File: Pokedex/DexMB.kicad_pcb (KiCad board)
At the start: 2 copper layers, 155.9 x 78.9 mm, 85 parts

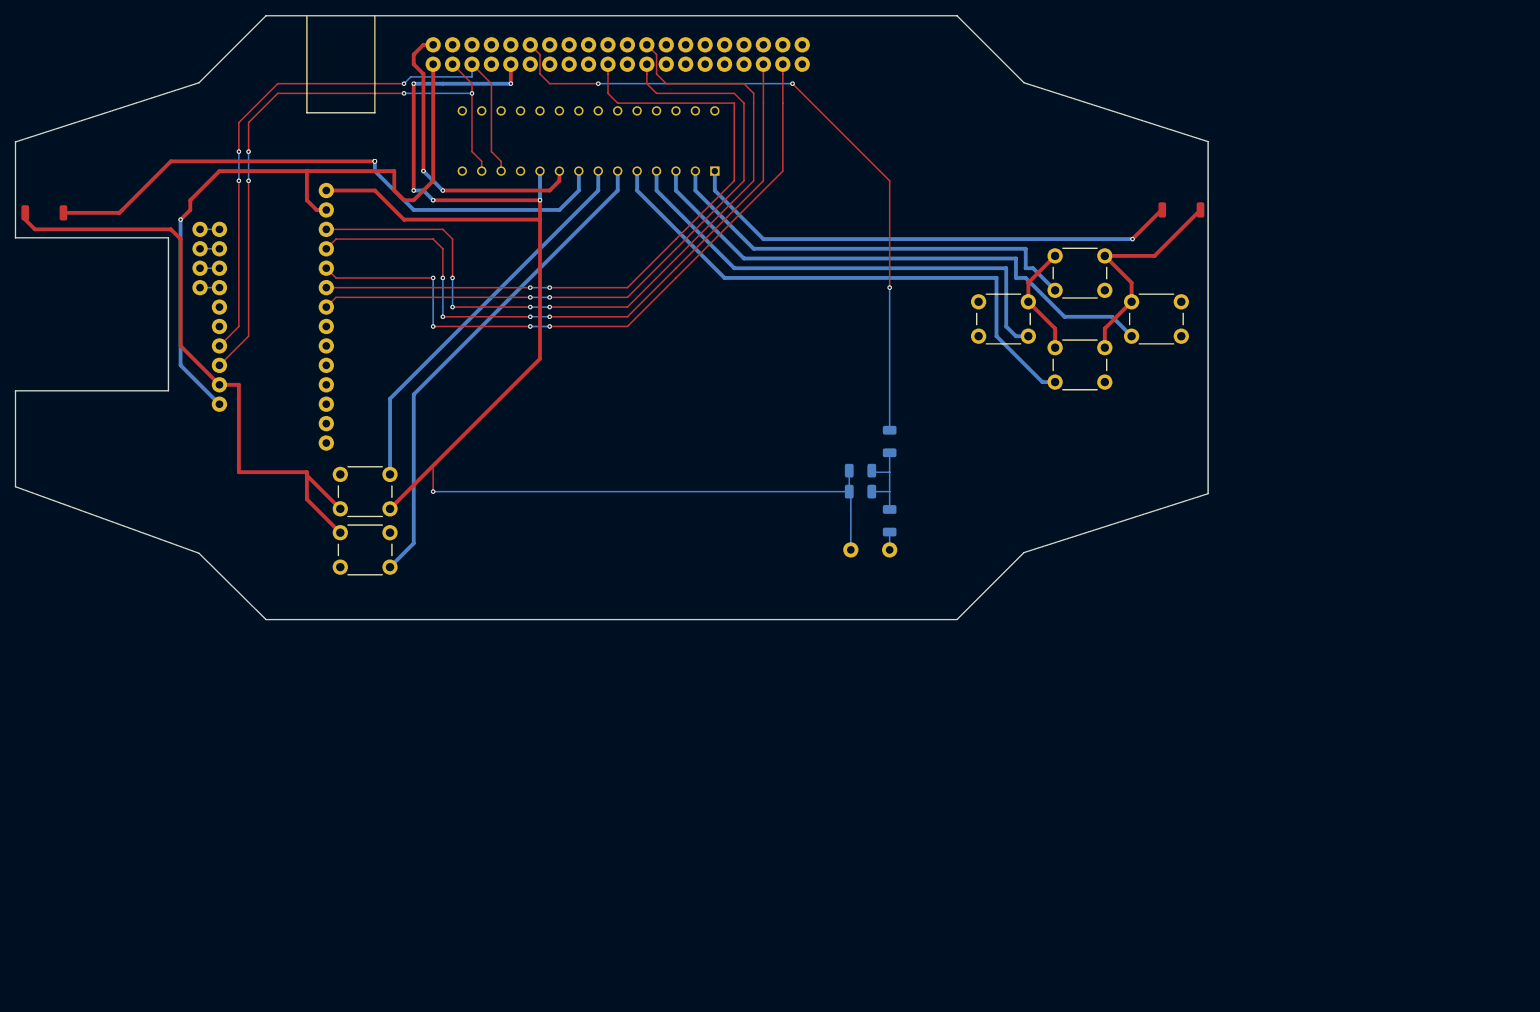
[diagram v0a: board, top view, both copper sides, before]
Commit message: Complete redesign progress and slimming of Motherboard
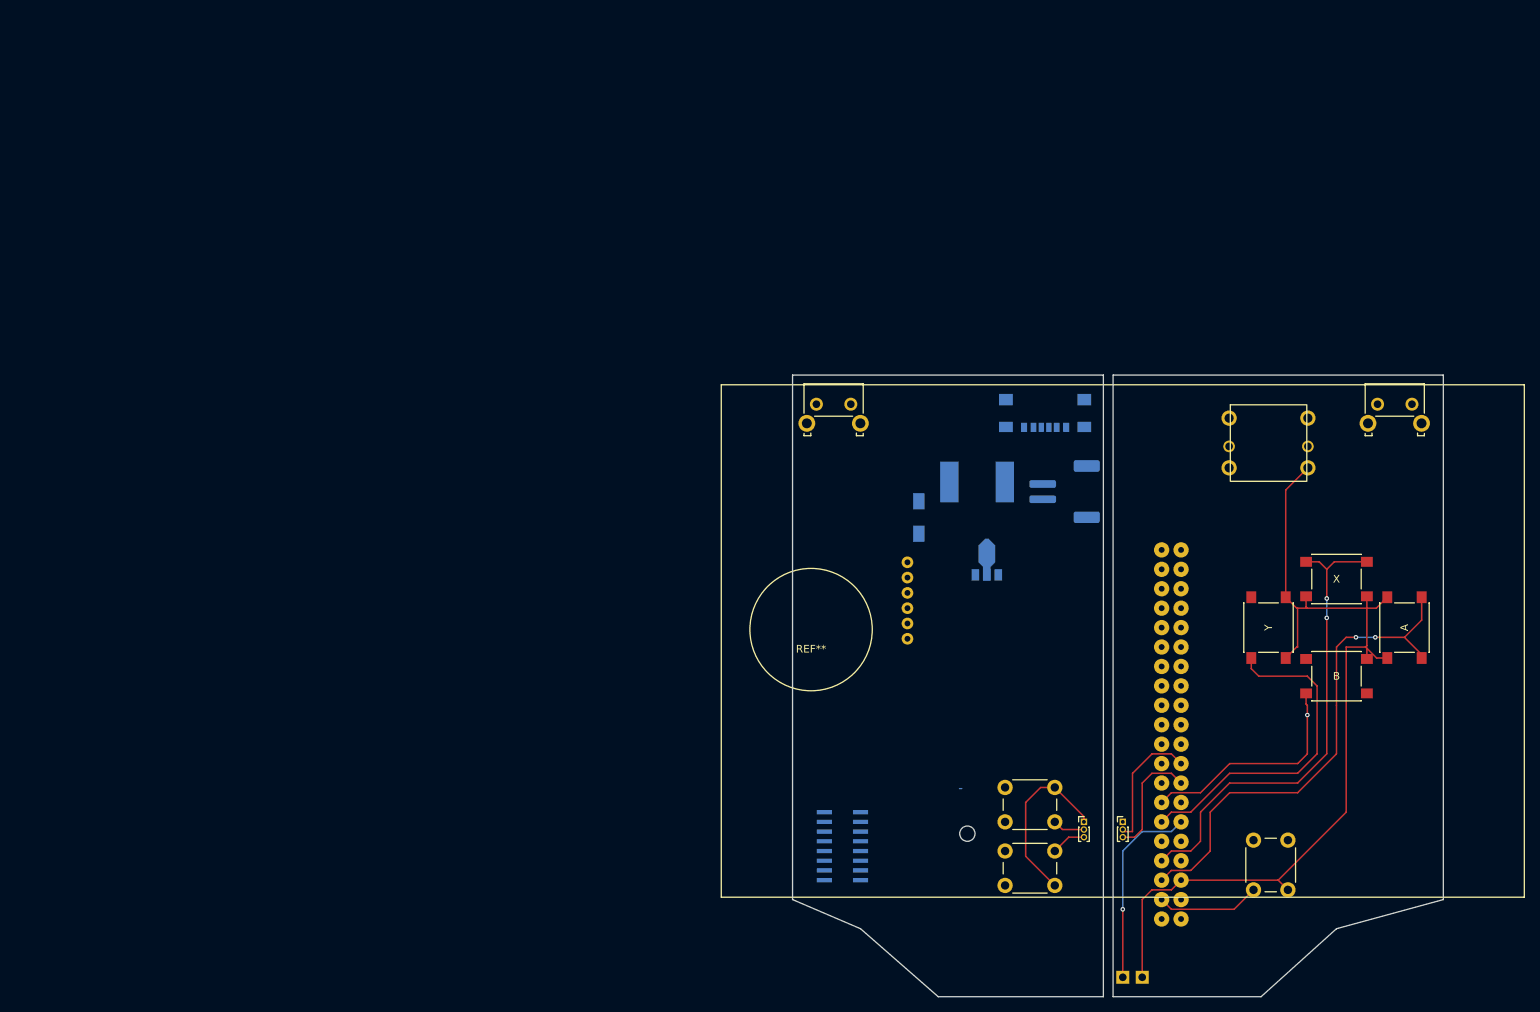
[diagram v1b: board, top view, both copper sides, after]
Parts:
- removed the ? at (39.4, 58.4)
- removed the ? at (36.8, 45.7)
- removed the ? at (92.7, 16.5)
- removed the ? at (162.6, 38.1)
- removed the ? at (74.9, 19.1)
- removed the ? at (85.1, 19.1)
- removed the ? at (67.3, 16.5)
- removed the ? at (53.3, 38.1)
- removed the ? at (72.4, 16.5)
- removed the ? at (39.4, 53.3)
- removed the ? at (39.4, 48.3)
- removed the ? at (105.4, 19.1)
- removed the ? at (39.4, 61.0)
- removed the ? at (53.3, 58.4)
- removed the ? at (85.1, 16.5)
- removed the ? at (53.3, 66.0)
- removed the ? at (110.5, 19.1)
- removed the ? at (90.2, 16.5)
- removed the ? at (80.0, 19.1)
- removed the ? at (115.6, 19.1)
- removed the ? at (121.9, 82.5)
- removed the ? at (14.0, 30.5)
- removed the ? at (97.8, 16.5)
- removed the ? at (87.6, 16.5)
- removed the ? at (95.2, 16.5)
- removed the ? at (39.4, 40.6)
- removed the ? at (17.8, 30.5)
- removed the ? at (167.6, 38.1)
- removed the ? at (108.0, 16.5)
- removed the ? at (69.8, 16.5)
- removed the ? at (53.3, 55.9)
- removed the ? at (53.3, 43.2)
- removed the ? at (53.3, 63.5)
- removed the ? at (39.4, 63.5)
- removed the ? at (82.5, 16.5)
- removed the ? at (87.6, 19.1)
- removed the ? at (67.3, 19.1)
- removed the ? at (39.4, 55.9)
- removed the ? at (53.3, 48.3)
- removed the ? at (100.3, 19.1)
- removed the ? at (92.7, 19.1)
- removed the ? at (39.4, 45.7)
- removed the ? at (39.4, 50.8)
- removed the ? at (95.2, 19.1)
- removed the ? at (127.0, 82.5)
- removed the ? at (53.3, 40.6)
- removed the ? at (115.6, 16.5)
- removed the ? at (53.3, 53.3)
- removed the ? at (77.5, 16.5)
- removed the ? at (77.5, 19.1)
- removed the ? at (100.3, 16.5)
- removed the ? at (53.3, 45.7)
- removed the ? at (53.3, 35.6)
- removed the ? at (102.9, 19.1)
- removed the ? at (105.4, 16.5)
- removed the ? at (36.8, 48.3)
- removed the ? at (82.5, 19.1)
- removed the ? at (69.8, 19.1)
- removed the ? at (74.9, 16.5)
- removed the ? at (80.0, 16.5)
- removed the ? at (53.3, 68.6)
- removed the ? at (39.4, 43.2)
- removed the ? at (72.4, 19.1)
- removed the ? at (113.0, 16.5)
- removed the ? at (102.9, 16.5)
- removed the ? at (97.8, 19.1)
- removed the ? at (110.5, 16.5)
- removed the ? at (36.8, 43.2)
- removed the ? at (53.3, 61.0)
- removed the ? at (108.0, 19.1)
- removed the ? at (113.0, 19.1)
- removed the ? at (36.8, 40.6)
- removed the ? at (90.2, 19.1)
- removed the ? at (53.3, 50.8)
- removed the REF** at (55.2, 72.7)
- removed the REF** at (87.6, 29.1)
- removed the REF** at (127.0, 68.4)
- removed the REF** at (55.2, 80.3)
- removed the REF** at (148.6, 56.1)
- removed the REF** at (158.6, 50.1)
- removed the REF** at (148.6, 44.1)
- removed the REF** at (138.6, 50.1)
- removed the REF** at (127.0, 78.7)
- removed the REF** at (123.2, 72.2)
- removed the REF** at (123.2, 74.9)
- added ?: , , F.Cu at (157.5, 138.4)
- added ?: , , F.Cu at (160.0, 138.4)
- added A: SW_Push_1P1T_NO_6x6mm_H9.5mm, Button_Switch_SMD:SW_Push_1P1T_NO_6x6mm_H9.5mm, F.Cu at (194.3, 92.7)
- added B: SW_Push_1P1T_NO_6x6mm_H9.5mm, Button_Switch_SMD:SW_Push_1P1T_NO_6x6mm_H9.5mm, F.Cu at (185.4, 99.1)
- added REF**: SW_Tactile_SKHH_Angled, Button_Switch_THT:SW_Tactile_SKHH_Angled, F.Cu at (190.8, 63.5)
- added REF**: JST_PH_S2B-PH-SM4-TB_1x02-1MP_P2.00mm_Horizontal, Connector_JST:JST_PH_S2B-PH-SM4-TB_1x02-1MP_P2.00mm_Horizontal, B.Cu at (149.9, 74.9)
- added REF**: CONV_ME2108A33P, Custom GBA Tools:CONV_ME2108A33P, B.Cu at (139.7, 83.8)
- added REF**: Pi GPIO Header, Custom GBA Tools:Pi GPIO Header, B.Cu at (162.6, 108.0)
- added REF**: MCP3008, Custom GBA Tools:MCP3008, B.Cu at (120.8, 121.3)
- added REF**: USB_C_Receptacle_GCT_USB4135-GF-A_6P_TopMnt_Horizontal, Connector_USB:USB_C_Receptacle_GCT_USB4135-GF-A_6P_TopMnt_Horizontal, B.Cu at (147.3, 63.5)
- added REF**: SS14_Diode, Custom GBA Tools:SS14_Diode, B.Cu at (130.8, 78.3)
- added REF**: IND_ETQP4M220KVK, Custom GBA Tools:IND_ETQP4M220KVK, B.Cu at (138.4, 73.7)
- added REF**: SW_Tactile_SKHH_Angled, Button_Switch_THT:SW_Tactile_SKHH_Angled, F.Cu at (117.4, 63.5)
- added REF**: Thru-hole joystick, Custom GBA Tools:Thru-hole joystick, F.Cu at (116.7, 93.0)
- added REF**: PinHeader_1x03_P1.00mm_Vertical, Connector_PinHeader_1.00mm:PinHeader_1x03_P1.00mm_Vertical, F.Cu at (157.5, 118.1)
- added REF**: SW_PUSH_6mm_H7.3mm, Button_Switch_THT:SW_PUSH_6mm_H7.3mm, F.Cu at (142.1, 121.9)
- added REF**: 4-way Directional Switch, Custom GBA Tools:4-way Directional Switch, F.Cu at (171.4, 65.3)
- added REF**: SW_PUSH_6mm_H7.3mm, Button_Switch_THT:SW_PUSH_6mm_H7.3mm, F.Cu at (142.1, 113.6)
- added REF**: SW_PUSH_6mm, Button_Switch_THT:SW_PUSH_6mm, F.Cu at (179.1, 120.5)
- added REF**: PinHeader_1x03_P1.00mm_Vertical, Connector_PinHeader_1.00mm:PinHeader_1x03_P1.00mm_Vertical, F.Cu at (152.4, 118.1)
- added X: SW_Push_1P1T_NO_6x6mm_H9.5mm, Button_Switch_SMD:SW_Push_1P1T_NO_6x6mm_H9.5mm, F.Cu at (185.4, 86.4)
- added Y: SW_Push_1P1T_NO_6x6mm_H9.5mm, Button_Switch_SMD:SW_Push_1P1T_NO_6x6mm_H9.5mm, F.Cu at (176.5, 92.7)
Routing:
- net (no net): track 1704.8 -> 425.9 mm, vias 38 -> 6
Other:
- board size 155.9 x 78.9 mm -> 85.1 x 81.3 mm
- board text removed: "3.3V"
- board text removed: "D/C"
- board text removed: "GND"
- board text removed: "GPB0"
- board text removed: "GPB1"
- board text removed: "GPB2"
- board text removed: "GPB3"
- board text removed: "GPB4"
- board text removed: "GPB5"
- board text removed: "GPB6"
- board text removed: "GPB7"
- board text removed: "MOSI"
- board text removed: "RST"
- board text removed: "SCL"
- board text removed: "SCLK"
- board text removed: "SDA"

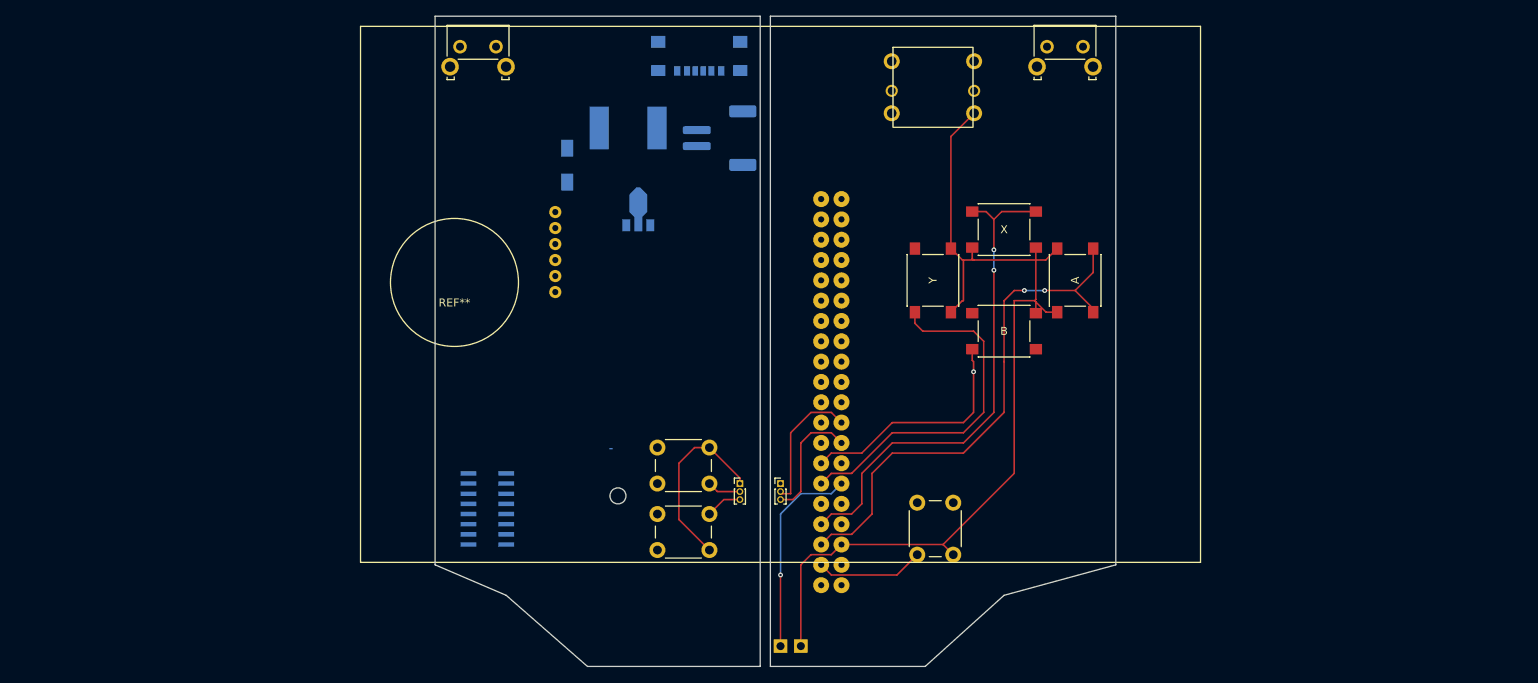
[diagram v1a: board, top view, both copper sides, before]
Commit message: Began Redesigned Motherboard
Began Motherboard Redesign to accomplish the following:
* Start laying out and including a 5V Buck boost on board
* power management for Pi and additional components
* 8-channel ADC for analog stick, Battery Percentage reporting to Pi
* Slim down board size to reduce fiberglass use and overall cost to produce
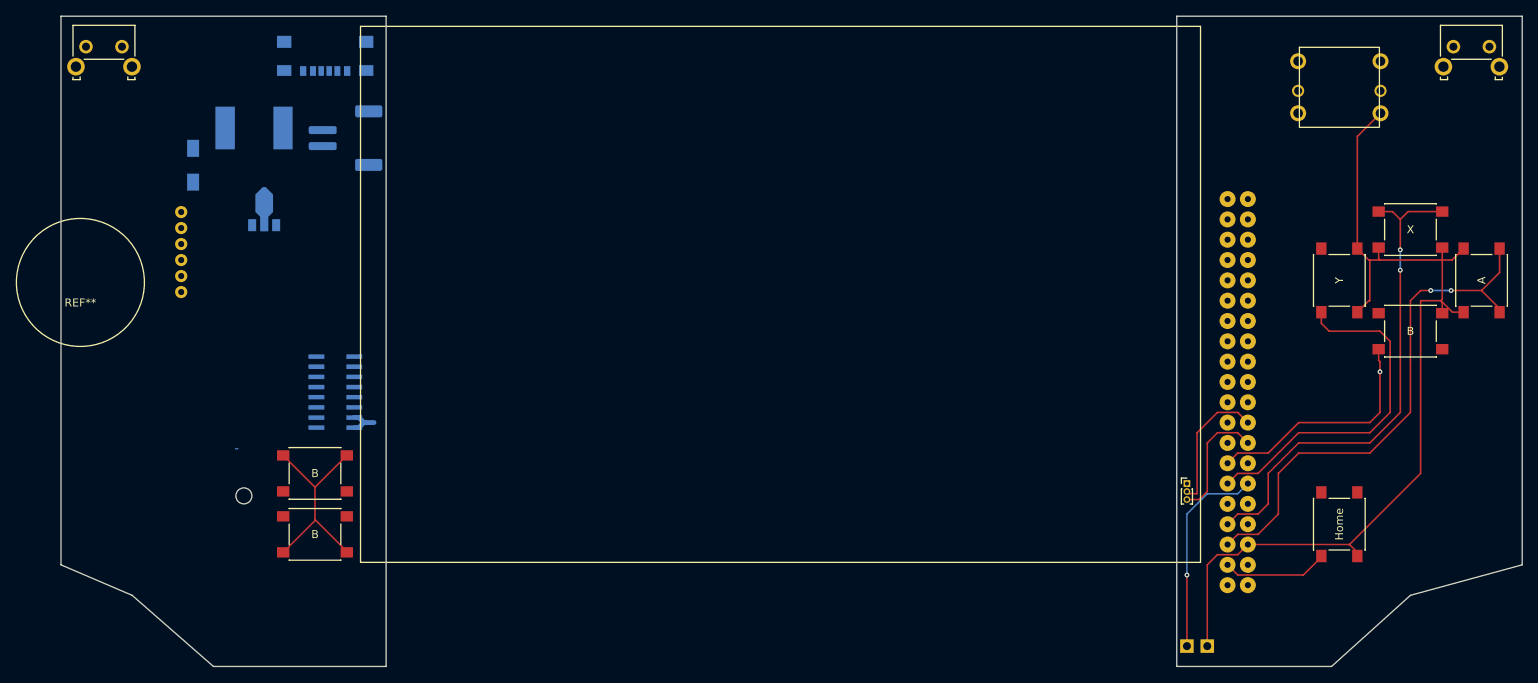
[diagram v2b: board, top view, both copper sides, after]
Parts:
- removed the REF** at (142.1, 121.9)
- removed the REF** at (142.1, 113.6)
- removed the REF** at (179.1, 120.5)
- removed the REF** at (152.4, 118.1)
- added B: SW_Push_1P1T_NO_6x6mm_H9.5mm, Button_Switch_SMD:SW_Push_1P1T_NO_6x6mm_H9.5mm, F.Cu at (99.3, 116.8)
- added B: SW_Push_1P1T_NO_6x6mm_H9.5mm, Button_Switch_SMD:SW_Push_1P1T_NO_6x6mm_H9.5mm, F.Cu at (99.3, 124.5)
- added Home: SW_Push_1P1T_NO_6x6mm_H9.5mm, Button_Switch_SMD:SW_Push_1P1T_NO_6x6mm_H9.5mm, F.Cu at (227.3, 123.2)
- moved ? 50.8 mm to (208.3, 138.4)
- moved A 50.8 mm to (245.1, 92.7)
- moved B 50.8 mm to (236.2, 99.1)
- moved REF** 50.8 mm to (241.6, 63.5)
- moved REF** 50.8 mm to (208.3, 118.1)
- moved REF** 50.8 mm to (222.2, 65.3)
- moved REF** 50.8 mm to (213.4, 108.0)
- moved X 50.8 mm to (236.2, 86.4)
- moved Y 50.8 mm to (227.3, 92.7)
- moved ? 50.8 mm to (210.8, 138.4)
- moved REF** 46.8 mm to (103.1, 74.9)
- moved REF** 46.8 mm to (84.0, 78.3)
- moved REF** 46.8 mm to (91.7, 73.7)
- moved REF** 46.8 mm to (70.7, 63.5)
- moved REF** 46.8 mm to (70.0, 93.0)
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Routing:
- net (no net): track 425.9 -> 424.7 mm
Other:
- board size 85.1 x 81.3 mm -> 182.6 x 81.3 mm
- board text added: "3.3V"

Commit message: 95% Complete Design
* Looking to add physical flip-flop switch in for power button
* Make pinouts for usb transfer
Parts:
- removed the REF** at (100.6, 63.5)
- removed the REF** at (84.0, 78.3)
- removed the REF** at (91.7, 73.7)
- removed the REF** at (208.3, 118.1)
- removed the REF** at (103.1, 74.9)
- removed the REF** at (92.9, 83.8)
- removed the REF** at (101.8, 106.7)
- added 150: R_0603_1608Metric, Resistor_SMD:R_0603_1608Metric, F.Cu at (231.8, 120.5)
- added 270: R_0603_1608Metric, Resistor_SMD:R_0603_1608Metric, F.Cu at (230.9, 118.1)
- added 33 nF: C_1206_3216Metric, Capacitor_SMD:C_1206_3216Metric, F.Cu at (235.6, 118.7)
- added ? (x2): , , F.Cu at (229.2, 123.2)
- added ?: , , F.Cu at (229.2, 125.1)
- added ADS1115: ADS1115, Custom GBA Tools:MSOP10, F.Cu at (89.3, 81.9)
- added B_Sav: Battery Protection Module, Custom GBA Tools:Battery Protection Module, B.Cu at (97.2, 141.0)
- added Bat_Man: Battery Charger Board, Custom GBA Tools:Battery Charger Board, B.Cu at (78.8, 104.8)
- added Battery: JST_EH_S2B-EH_1x02_P2.50mm_Horizontal, Connector_JST:JST_EH_S2B-EH_1x02_P2.50mm_Horizontal, B.Cu at (97.3, 109.8)
- added FPC: Molex_200528-0140_1x14-1MP_P1.00mm_Horizontal, Connector_FFC-FPC:Molex_200528-0140_1x14-1MP_P1.00mm_Horizontal, F.Cu at (208.3, 124.2)
- added FPC: Molex_200528-0140_1x14-1MP_P1.00mm_Horizontal, Connector_FFC-FPC:Molex_200528-0140_1x14-1MP_P1.00mm_Horizontal, F.Cu at (101.6, 86.4)
- added REF**: SW_Tactile_SKHH_Angled, Button_Switch_THT:SW_Tactile_SKHH_Angled, F.Cu at (90.2, 54.7)
- added REF**: SW_Tactile_SKHH_Angled, Button_Switch_THT:SW_Tactile_SKHH_Angled, F.Cu at (106.0, 54.7)
- added REF**: SW_Tactile_SKHH_Angled, Button_Switch_THT:SW_Tactile_SKHH_Angled, F.Cu at (116.2, 54.7)
- added REF**: JST_PH_B2B-PH-K_1x02_P2.00mm_Vertical, Connector_JST:JST_PH_B2B-PH-K_1x02_P2.00mm_Vertical, F.Cu at (220.7, 112.6)
- added USB C: USB_C_Receptacle_G-Switch_GT-USB-7010ASV, Connector_USB:USB_C_Receptacle_G-Switch_GT-USB-7010ASV, B.Cu at (102.3, 137.8)
- moved ? 26.5 mm to (231.1, 125.1)
- moved ? 25.4 mm to (231.1, 123.2)
- moved REF** 16.0 mm to (54.8, 65.2)
- moved REF** 12.0 mm to (253.4, 65.3)
- moved Home 3.81 mm to (223.5, 123.2)
- renumbered B to SELECT, B to START
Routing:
- net (no net): track 424.7 -> 1644.5 mm, vias 6 -> 48
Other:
- board size 182.6 x 81.3 mm -> 208.7 x 88.9 mm
- board text added: "GND"
- board text added: "VCC"
- board text removed: "3.3V"
